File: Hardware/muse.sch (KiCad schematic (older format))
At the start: 44 parts

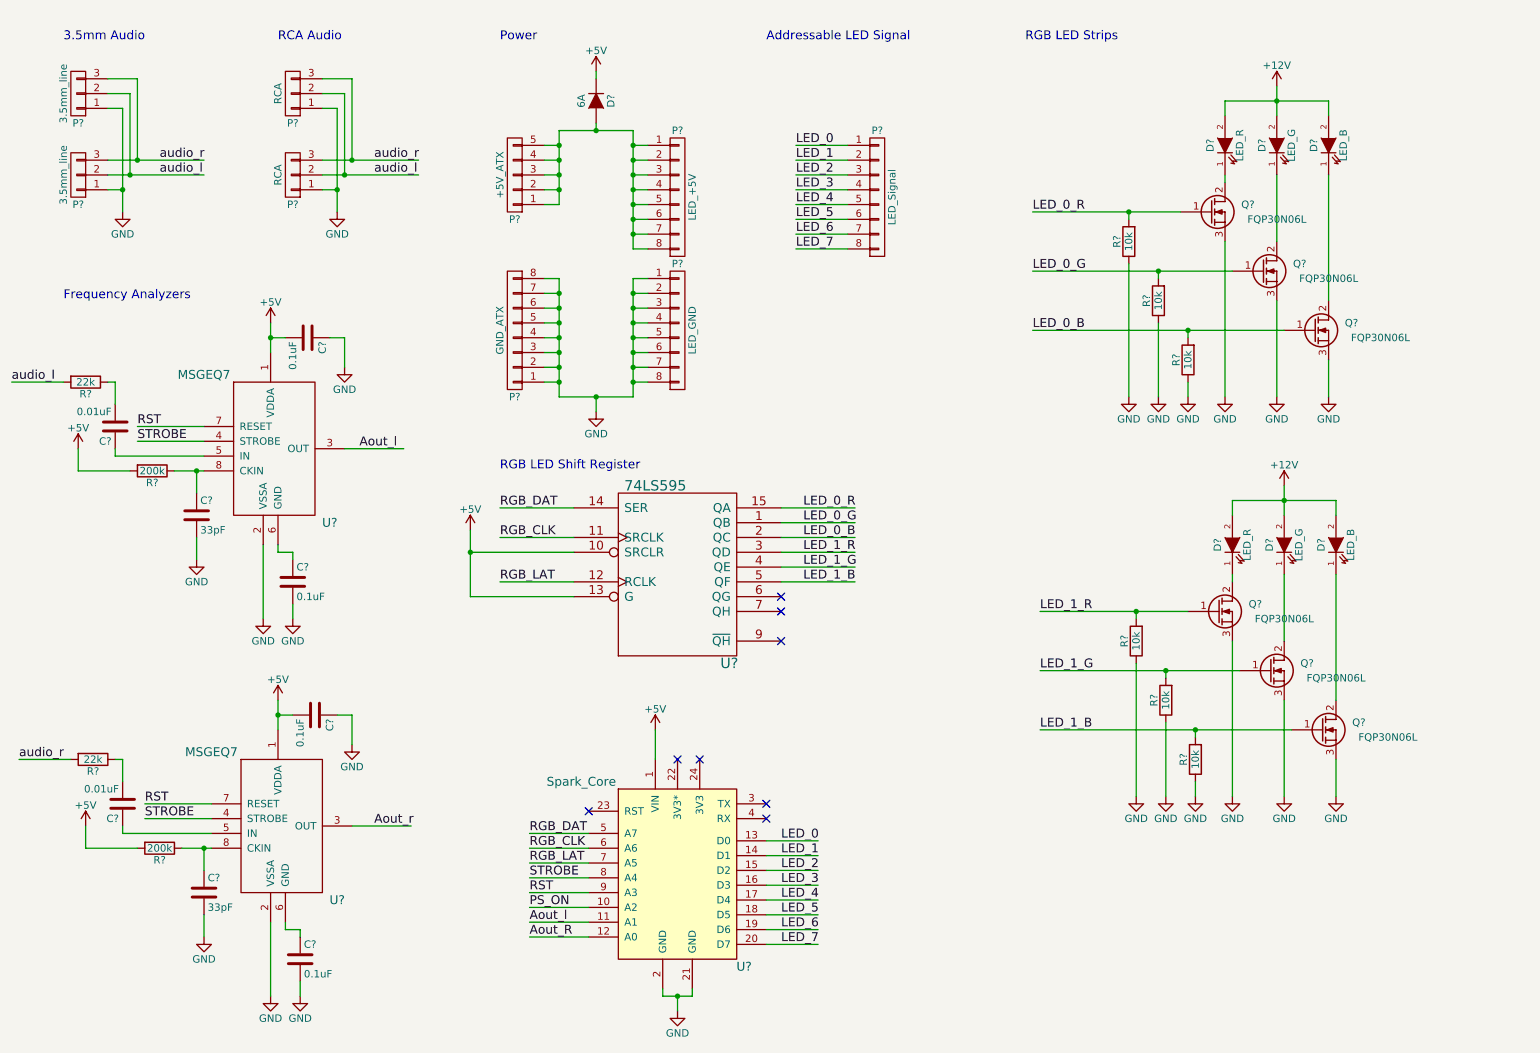
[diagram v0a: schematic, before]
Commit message: Added Power Switch (v1 complete)
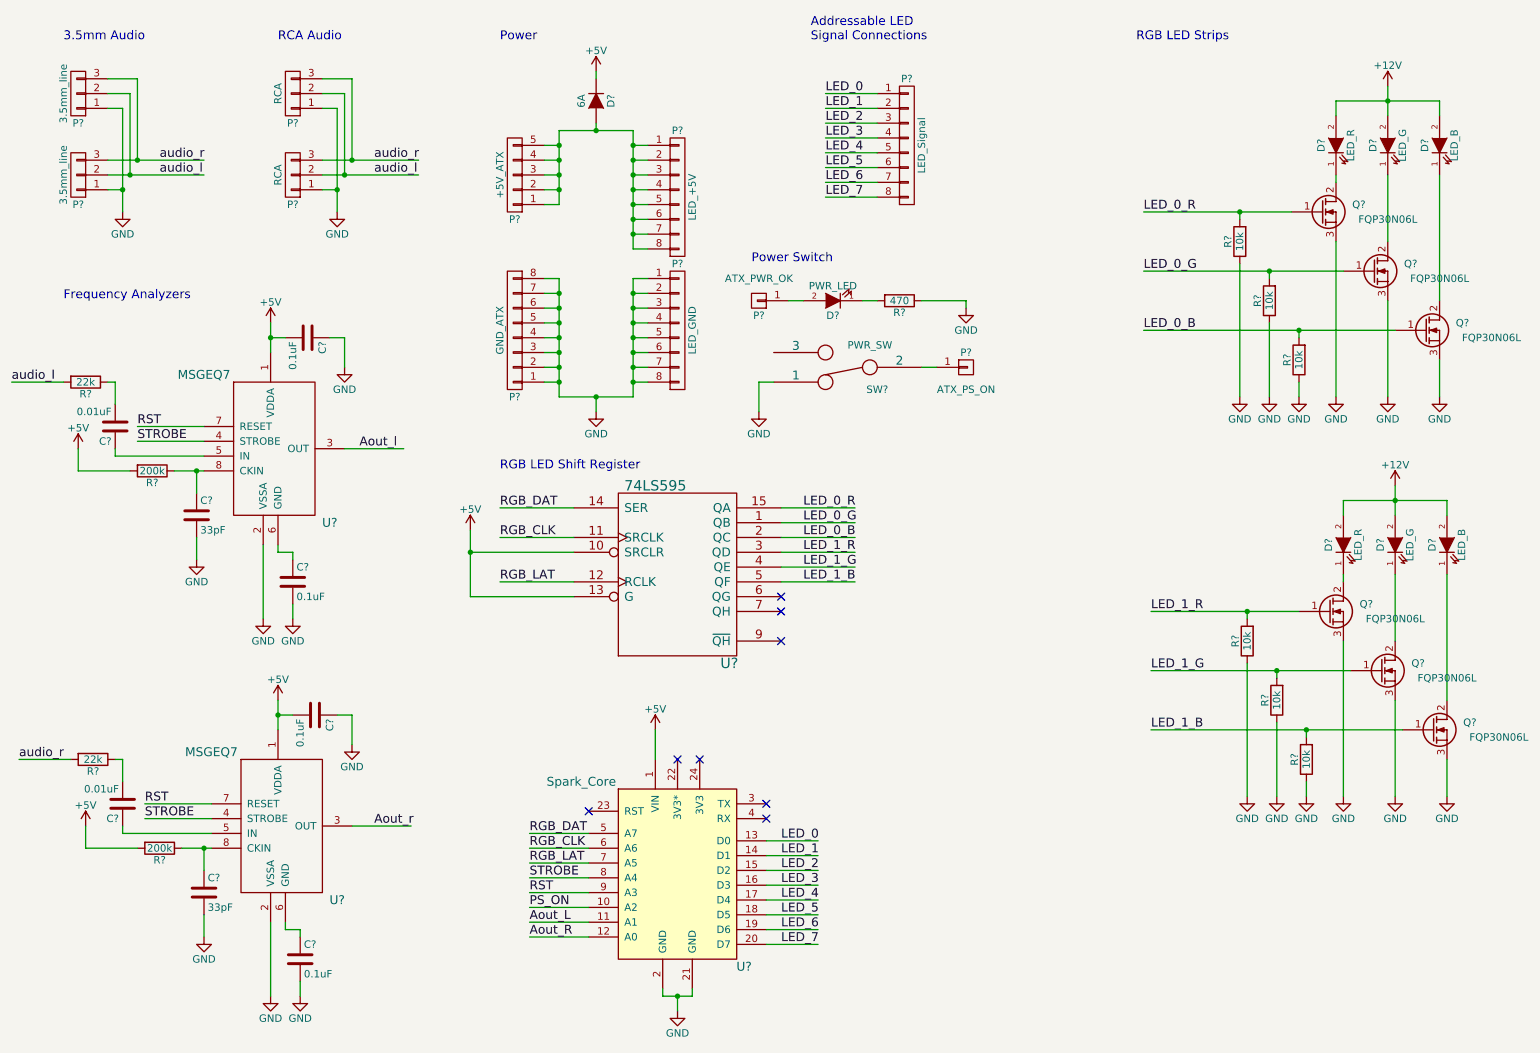
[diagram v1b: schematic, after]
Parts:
- added D?: PWR_LED, symbol LED
- added P?: ATX_PS_ON, symbol CONN_01X01
- added P?: ATX_PWR_OK, symbol CONN_01X01
- added R?: 470, symbol R
- added SW?: PWR_SW, symbol SWITCH_INV
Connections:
- net labels added: Aout_L
- wire segments 228 -> 186
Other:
- note added: "Addressable LED\nSignal Connections"
- note added: "Power Switch"
- note removed: "Addressable LED Signal"
- moved on the sheet: D?, P?, Q?, R?

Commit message: Updated power distibution
Removed onboard power routing to allow for high current wire to be
added directly to terminal block.
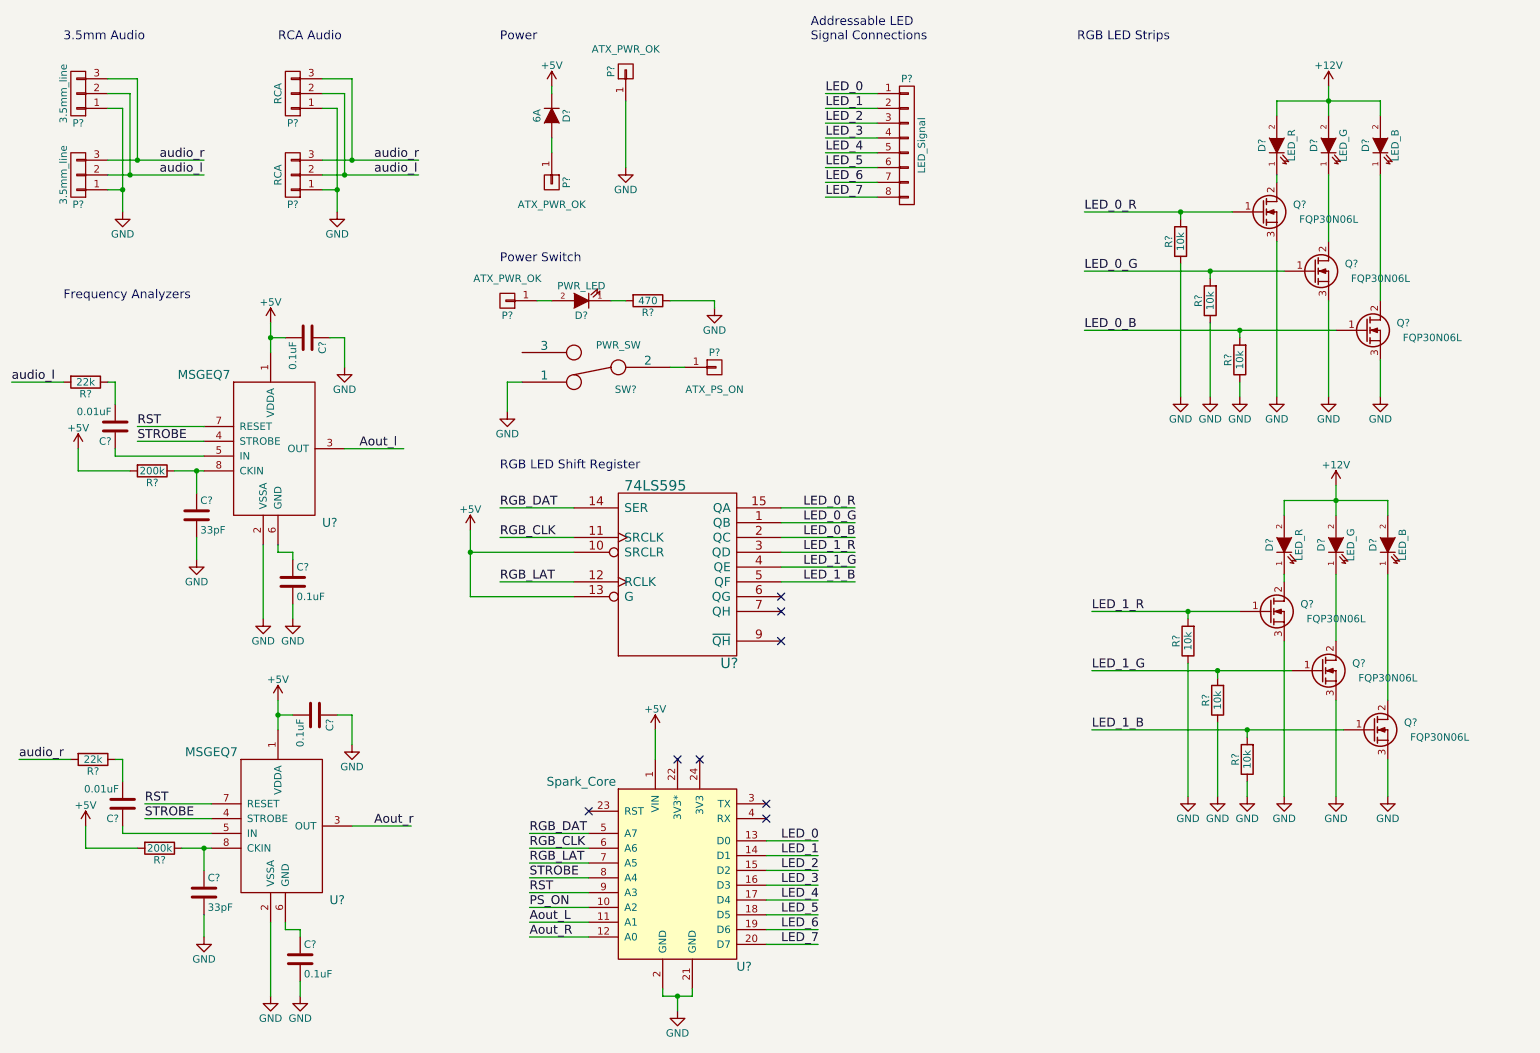
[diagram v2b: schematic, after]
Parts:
- removed P?: +5V_ATX, symbol CONN_01X05
- removed P?: LED_+5V, symbol CONN_01X08
- removed P?: GND_ATX, symbol CONN_01X08
- removed P?: LED_GND, symbol CONN_01X08
- added P? (x2): ATX_PWR_OK, symbol CONN_01X01
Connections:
- wire segments 186 -> 173
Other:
- moved on the sheet: D?, P?, Q?, R?, SW?
